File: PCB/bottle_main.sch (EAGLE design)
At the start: 0 parts

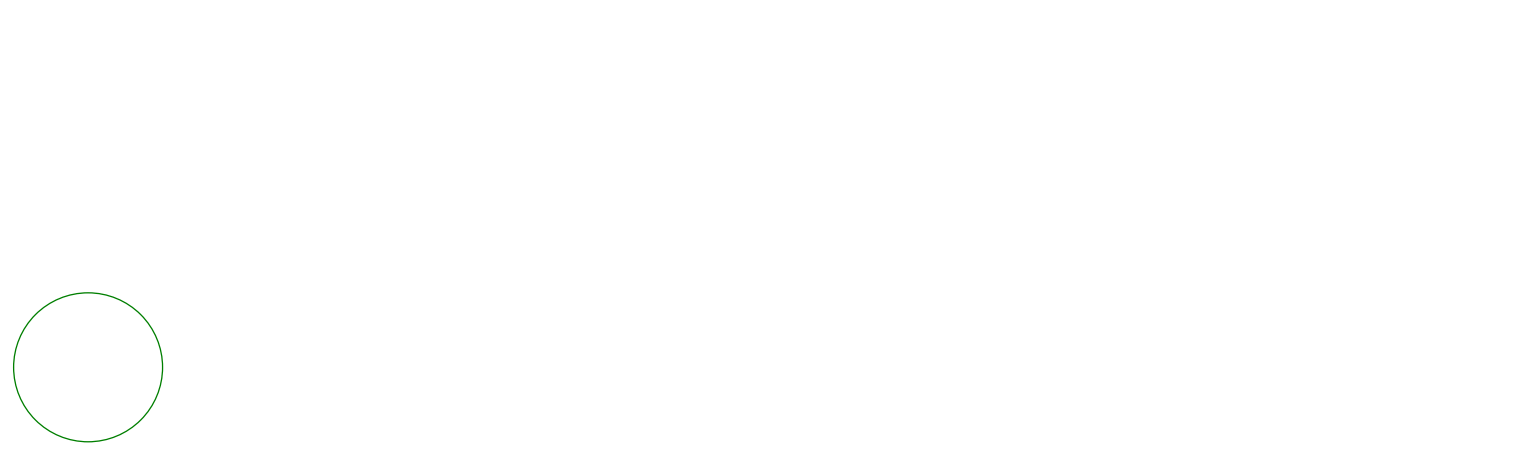
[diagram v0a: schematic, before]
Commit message: v 0.01
The first draft of arduino program for the smartbottle
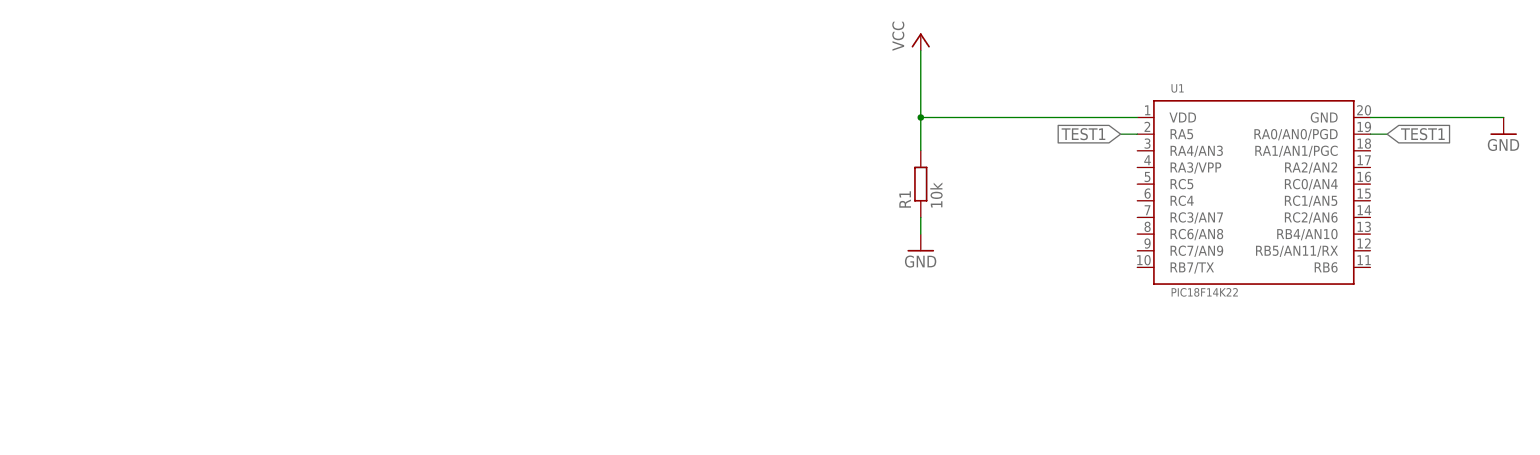
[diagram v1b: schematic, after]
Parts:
- added R1: 10k, resistor:R-EU_R0805
- added U1: PIC18F14K22, shaporev:PIC18F1XKXX
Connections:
- new net GND: R1.1, U1.GND
- new net TEST1: U1.RA0/AN0/PGD, U1.RA5
- new net VDD: R1.2, U1.VDD
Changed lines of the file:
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@@
 <grid distance="0.1" unitdist="inch" unit="inch" style="lines" multiple="1" display="no" altdistance="0.01" altunitdist="inch" altunit="inch"/>
 <layers>
+<layer number="1" name="Top" color="4" fill="1" visible="no" active="no"/>
+<layer number="16" name="Bottom" color="1" fill="1" visible="no" active="no"/>
+<layer number="17" name="Pads" color="2" fill="1" visible="no" active="no"/>
+<layer number="18" name="Vias" color="2" fill="1" visible="no" active="no"/>
+<layer number="19" name="Unrouted" color="6" fill="1" visible="no" active="no"/>
+<layer number="20" name="Dimension" color="15" fill="1" visible="no" active="no"/>
+<layer number="21" name="tPlace" color="7" fill="1" visible="no" active="no"/>
+<layer number="22" name="bPlace" color="7" fill="1" visible="no" active="no"/>
+<layer number="23" name="tOrigins" color="15" fill="1" visible="no" active="no"/>
+<layer number="24" name="bOrigins" color="15" fill="1" visible="no" active="no"/>
+<layer number="25" name="tNames" color="7" fill="1" visible="no" active="no"/>
+<layer number="26" name="bNames" color="7" fill="1" visible="no" active="no"/>
+<layer number="27" name="tValues" color="7" fill="1" visible="no" active="no"/>
+<layer number="28" name="bValues" color="7" fill="1" visible="no" active="no"/>
+<layer number="29" name="tStop" color="7" fill="3" visible="no" active="no"/>
+<layer number="30" name="bStop" color="7" fill="6" visible="no" active="no"/>
+<layer number="31" name="tCream" color="7" fill="4" visible="no" active="no"/>
+<layer number="32" name="bCream" color="7" fill="5" visible="no" active="no"/>
+<layer number="33" name="tFinish" color="6" fill="3" visible="no" active="no"/>
+<layer number="34" name="bFinish" color="6" fill="6" visible="no" active="no"/>
+<layer number="35" name="tGlue" color="7" fill="4" visible="no" active="no"/>
+<layer number="36" name="bGlue" color="7" fill="5" visible="no" active="no"/>
+<layer number="37" name="tTest" color="7" fill="1" visible="no" active="no"/>
+<layer number="38" name="bTest" color="7" fill="1" visible="no" active="no"/>
+<layer number="39" name="tKeepout" color="4" fill="11" visible="no" active="no"/>
+<layer number="40" name="bKeepout" color="1" fill="11" visible="no" active="no"/>
+<layer number="41" name="tRestrict" color="4" fill="10" visible="no" active="no"/>
+<layer number="42" name="bRestrict" color="1" fill="10" visible="no" active="no"/>
+<layer number="43" name="vRestrict" color="2" fill="10" visible="no" active="no"/>
+<layer number="44" name="Drills" color="7" fill="1" visible="no" active="no"/>
+<layer number="45" name="Holes" color="7" fill="1" visible="no" active="no"/>
+<layer number="46" name="Milling" color="3" fill="1" visible="no" active="no"/>
+<layer number="47" name="Measures" color="7" fill="1" visible="no" active="no"/>
+<layer number="48" name="Document" color="7" fill="1" visible="no" active="no"/>
+<layer number="49" name="Reference" color="7" fill="1" visible="no" active="no"/>
+<layer number="50" name="dxf" color="7" fill="1" visible="no" active="no"/>
+<layer number="51" name="tDocu" color="7" fill="1" visible="no" active="no"/>
+<layer number="52" name="bDocu" color="7" fill="1" visible="no" active="no"/>
+<layer number="53" name="tGND_GNDA" color="7" fill="9" visible="no" active="no"/>
+<layer number="54" name="bGND_GNDA" color="1" fill="9" visible="no" active="no"/>
+<layer number="56" name="wert" color="7" fill="1" visible="no" active="no"/>
 <layer number="91" name="Nets" color="2" fill="1" visible="yes" active="yes"/>
 <layer number="92" name="Busses" color="1" fill="1" visible="yes" active="yes"/>
@@
 <layer number="97" name="Info" color="7" fill="1" visible="yes" active="yes"/>
 <layer number="98" name="Guide" color="6" fill="1" visible="yes" active="yes"/>
+<layer number="100" name="Muster" color="7" fill="1" visible="no" active="no"/>
+<layer number="101" name="Patch_Top" color="12" fill="4" visible="no" active="yes"/>
+<layer number="102" name="Vscore" color="7" fill="1" visible="no" active="yes"/>
+<layer number="103" name="tMap" color="7" fill="1" visible="no" active="yes"/>
+<layer number="104" name="Name" color="16" fill="1" visible="yes" active="yes"/>
+<layer number="105" name="tPlate" color="7" fill="1" visible="no" active="yes"/>
+<layer number="106" name="bPlate" color="7" fill="1" visible="no" active="yes"/>
+<layer number="107" name="Crop" color="7" fill="1" visible="no" active="yes"/>
+<layer number="116" name="Patch_BOT" color="9" fill="4" visible="no" active="yes"/>
+<layer number="121" name="_tsilk" color="7" fill="1" visible="no" active="yes"/>
+<layer number="122" name="_bsilk" color="7" fill="1" visible="no" active="yes"/>
+<layer number="125" name="_tNames" color="7" fill="1" visible="no" active="yes"/>
+<layer number="144" name="Drill_legend" color="7" fill="1" visible="no" active="yes"/>
+<layer number="151" name="HeatSink" color="7" fill="1" visible="no" active="yes"/>
+<layer number="200" name="200bmp" color="1" fill="10" visible="no" active="yes"/>
+<layer number="201" name="201bmp" color="2" fill="10" visible="no" active="yes"/>
+<layer number="202" name="202bmp" color="3" fill="10" visible="no" active="yes"/>
+<layer number="203" name="203bmp" color="4" fill="10" visible="no" active="yes"/>
+<layer number="204" name="204bmp" color="5" fill="10" visible="no" active="yes"/>
+<layer number="205" name="205bmp" color="6" fill="10" visible="no" active="yes"/>
+<layer number="206" name="206bmp" color="7" fill="10" visible="no" active="yes"/>
+<layer number="207" name="207bmp" color="8" fill="10" visible="no" active="yes"/>
+<layer number="208" name="208bmp" color="9" fill="10" visible="no" active="yes"/>
+<layer number="209" name="209bmp" color="7" fill="1" visible="no" active="yes"/>
+<layer number="210" name="210bmp" color="7" fill="1" visible="no" active="yes"/>
+<layer number="211" name="211bmp" color="7" fill="1" visible="no" active="yes"/>
+<layer number="212" name="212bmp" color="7" fill="1" visible="no" active="yes"/>
+<layer number="213" name="213bmp" color="7" fill="1" visible="no" active="yes"/>
+<layer number="214" name="214bmp" color="7" fill="1" visible="no" active="yes"/>
+<layer number="215" name="215bmp" color="7" fill="1" visible="no" active="yes"/>
+<layer number="216" name="216bmp" color="7" fill="1" visible="no" active="yes"/>
+<layer number="217" name="217bmp" color="18" fill="1" visible="no" active="no"/>
+<layer number="218" name="218bmp" color="19" fill="1" visible="no" active="no"/>
+<layer number="219" name="219bmp" color="20" fill="1" visible="no" active="no"/>
+<layer number="220" name="220bmp" color="21" fill="1" visible="no" active="no"/>
+<layer number="221" name="221bmp" color="22" fill="1" visible="no" active="no"/>
+<layer number="222" name="222bmp" color="23" fill="1" visible="no" active="no"/>
+<layer number="223" name="223bmp" color="24" fill="1" visible="no" active="no"/>
+<layer number="224" name="224bmp" color="25" fill="1" visible="no" active="no"/>
+<layer number="250" name="Descript" color="3" fill="1" visible="no" active="no"/>
+<layer number="251" name="SMDround" color="12" fill="11" visible="no" active="no"/>
+<layer number="254" name="cooling" color="7" fill="1" visible="no" active="yes"/>
 </layers>
 <schematic xreflabel="%F%N/%S.%C%R" xrefpart="/%S.%C%R">
 <attributes>
+<attribute name="AUTHOR" value="Aleksey Shaporev"/>
+<attribute name="DRAWING_AUTHOR" value="Aleksey Shaporev"/>
+<attribute name="DRAWING_COMPANY" value="Clemson University"/>
+<attribute name="REVISION" value="0.0"/>
 </attributes>
 <variantdefs>
@@
 </classes>
 <parts>
+<part name="FRAME1" library="shaporev" deviceset="A4L-LOC" device=""/>
+<part name="P+1" library="supply1" deviceset="VCC" device=""/>
+<part name="GND1" library="supply1" deviceset="GND" device=""/>
+<part name="GND2" library="supply1" deviceset="GND" device=""/>
+<part name="U1" library="shaporev" deviceset="PIC18F1XKXX" device="" value="PIC18F14K22"/>
+<part name="R1" library="resistor" deviceset="R-EU_" device="R0805" value="10k"/>
 </parts>
 <sheets>
 <sheet>
 <plain>
-<circle x="0" y="66.04" radius="11.359225" width="0.1524" layer="91"/>
 </plain>
 <instances>
+<instance part="FRAME1" gate="G$1" x="0" y="0"/>
+<instance part="P+1" gate="VCC" x="127" y="116.84"/>
+<instance part="GND1" gate="1" x="127" y="83.82"/>
+<instance part="GND2" gate="1" x="215.9" y="101.6"/>
+<instance part="U1" gate="G$1" x="177.8" y="93.98"/>
+<instance part="R1" gate="G$1" x="127" y="93.98" rot="R90"/>
 </instances>
 <busses>
 </busses>
 <nets>
+<net name="VDD" class="0">
+<segment>
+<pinref part="P+1" gate="VCC" pin="VCC"/>
+<wire x1="127" y1="114.3" x2="127" y2="104.14" width="0.1524" layer="91"/>
+<pinref part="U1" gate="G$1" pin="VDD"/>
+<wire x1="127" y1="104.14" x2="127" y2="99.06" width="0.1524" layer="91"/>
+<wire x1="160.02" y1="104.14" x2="127" y2="104.14" width="0.1524" layer="91"/>
+<junction x="127" y="104.14"/>
+<pinref part="R1" gate="G$1" pin="2"/>
+</segment>
+</net>
+<net name="GND" class="0">
+<segment>
+<pinref part="GND1" gate="1" pin="GND"/>
+<wire x1="127" y1="88.9" x2="127" y2="86.36" width="0.1524" layer="91"/>
+<pinref part="R1" gate="G$1" pin="1"/>
+</segment>
+<segment>
+<pinref part="U1" gate="G$1" pin="GND"/>
+<wire x1="195.58" y1="104.14" x2="215.9" y2="104.14" width="0.1524" layer="91"/>
+<pinref part="GND2" gate="1" pin="GND"/>
+</segment>
+</net>
+<net name="TEST1" class="0">
+<segment>
+<pinref part="U1" gate="G$1" pin="RA5"/>
+<wire x1="160.02" y1="101.6" x2="157.48" y2="101.6" width="0.1524" layer="91"/>
+<label x="157.48" y="101.6" size="1.778" layer="95" rot="R180" xref="yes"/>
+</segment>
+<segment>
+<pinref part="U1" gate="G$1" pin="RA0/AN0/PGD"/>
+<wire x1="195.58" y1="101.6" x2="198.12" y2="101.6" width="0.1524" layer="91"/>
+<label x="198.12" y="101.6" size="1.778" layer="95" xref="yes"/>
+</segment>
+</net>
 </nets>
 </sheet>
